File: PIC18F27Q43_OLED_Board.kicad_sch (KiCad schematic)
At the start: 29 parts, among them J1 Conn_PIC_ICSP_ICD, J2 OLED_Connector, J3 UART_Connector, SW1 SW_Push, SW2 SW_Push, SW3 SW_Push, SW4 SW_SPDT, SW5 SW_SPDT, SW6 SW_SPDT, SW7 SW_SPDT, U1 PIC18F27Q43-I/STX

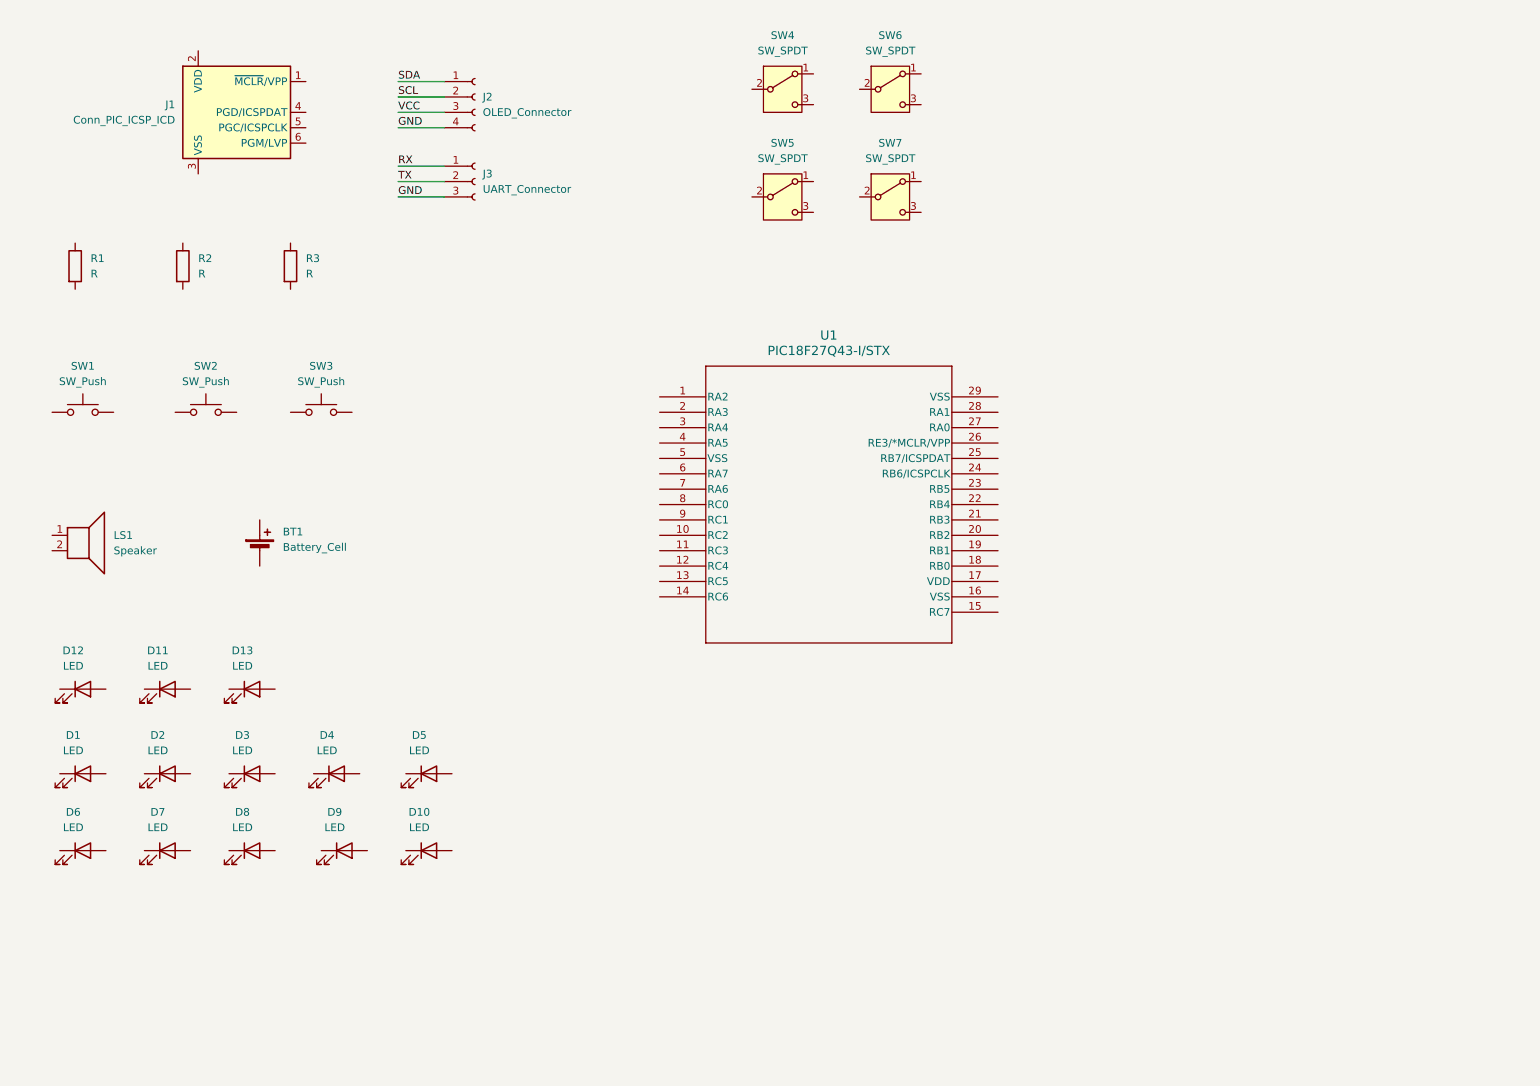
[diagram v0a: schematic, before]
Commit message: Finished SCHfor VEXT + VBAT
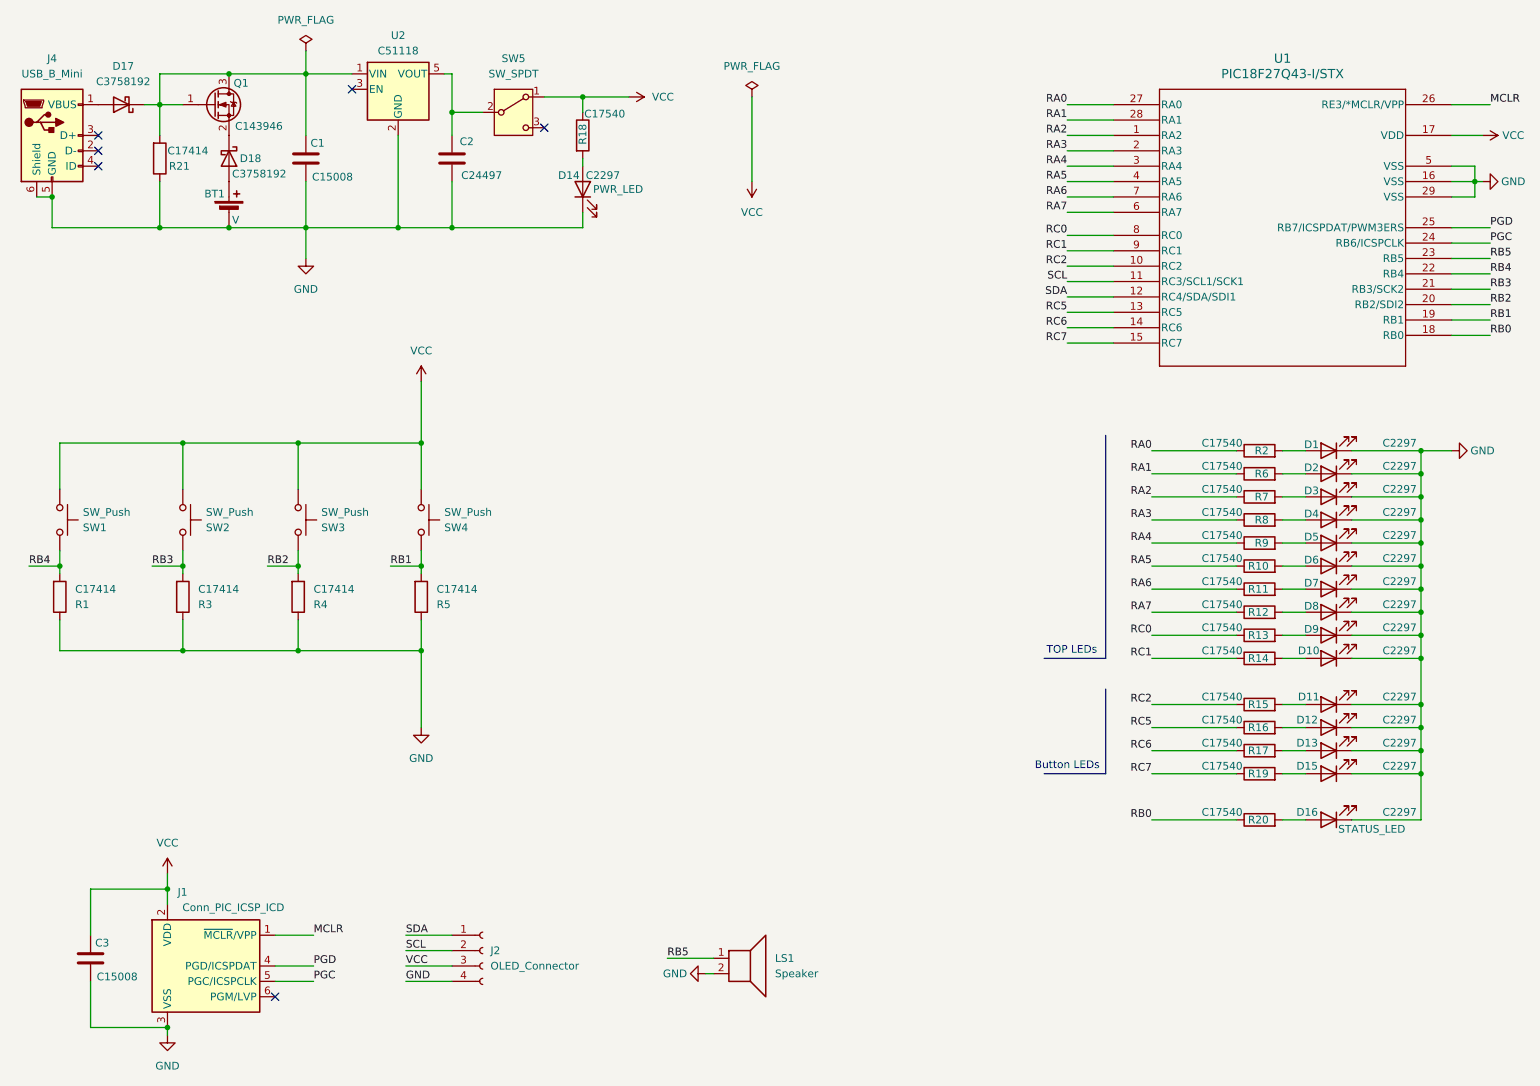
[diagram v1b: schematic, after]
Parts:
- removed J3: UART_Connector, symbol Connector:Conn_01x03_Socket
- removed SW5, SW6, SW7: SW_SPDT, symbol Switch:SW_SPDT
- added C1, C3: C15008, Capacitor_SMD:C_1206_3216Metric, symbol Device:C
- added C2: C24497, Capacitor_SMD:C_1206_3216Metric, symbol Device:C
- added D14, D15, D16: C2297, LED_0805_2012Metric, symbol Device:LED
- added D17, D18: C3758192, Diode_SMD:D_0603_1608Metric, symbol Device:D_Schottky
- added J4: USB_B_Mini, Connector_USB:USB_Mini-B_Tensility_54-00023_Vertical, symbol Connector:USB_B_Mini
- added Q1: C143946, Package_TO_SOT_SMD:SOT-23, symbol Transistor_FET:IRLML6244
- added R10, R11, R12, R13, R14, R15, R16, R17, R18, R19, R20, R6, R7, R8, R9: C17540, Resistor_SMD:R_0805_2012Metric, symbol Device:R
- added R21, R4, R5: C17414, Resistor_SMD:R_0805_2012Metric, symbol Device:R
- added SW4: SW_Push, Button_Switch_THT:SW_PUSH_6mm_H5mm, symbol Switch:SW_Push
- added U2: C51118, Package_TO_SOT_SMD:SOT-23-5, symbol Regulator_Linear:AP2112K-3.3
- BT1: value Battery_Cell -> V; footprint (none) -> Battery:BatteryHolder_ComfortableElectronic_CH273-2450_1x2450
- D1, D10, D11, D12, D13, D2, D3, D4, D5, D6, D7, D8, D9: value LED -> C2297; footprint (none) -> LED_0805_2012Metric
- J1: footprint (none) -> Connector_PinHeader_2.54mm:PinHeader_1x05_P2.54mm_Vertical
- J2: footprint (none) -> Connector_PinHeader_2.54mm:PinHeader_1x04_P2.54mm_Vertical
- LS1: footprint (none) -> Buzzer_Beeper:Buzzer_12x9.5RM7.6
- R1, R3: value R -> C17414; footprint (none) -> Resistor_SMD:R_0805_2012Metric
- R2: value R -> C17540; footprint (none) -> Resistor_SMD:R_0805_2012Metric
- SW1, SW2, SW3: footprint (none) -> Button_Switch_THT:SW_PUSH_6mm_H5mm
- SW5: renamed from SW4; footprint (none) -> Button_Switch_THT:SW_Slide_SPDT_Straight_CK_OS102011MS2Q
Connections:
- net GND: now also BT1.2 (-), D1.1 (K), D10.1 (K), D11.1 (K), D12.1 (K), D13.1 (K), D2.1 (K), D3.1 (K), D4.1 (K), D5.1 (K), D6.1 (K), D7.1 (K), D8.1 (K), D9.1 (K), J1.3 (VSS), LS1.2, R1.1, R3.1, U1.16 (VSS), U1.29 (VSS), U1.5 (VSS), C1.2, C2.2, C3.2, D14.1 (K), D15.1 (K), D16.1 (K), J4.5 (GND), J4.6 (Shield), R21.1, R4.1, R5.1, U2.2 (GND)
- net SCL: now also U1.11 (RC3/SCL1/SCK1)
- net SDA: now also U1.12 (RC4/SDA/SDI1)
- net VCC: now also J1.2 (VDD), SW1.2, SW2.2, SW3.2, SW5.1 (A), U1.17 (VDD), C3.1, R18.1, SW4.2
- net RB2: now reaches SW3.1
- net RB2: now also U1.20 (RB2/SDI2), R4.2
- net at D9.2 (A): now also R13.2
- net RB4: now reaches SW1.1
- net RB4: now also R1.2, U1.22 (RB4)
- net RA2: now reaches U1.1 (RA2)
- net RA2: now also R7.1
- net RC2: now reaches U1.10 (RC2)
- net RC2: now also R15.1
- net RC5: now reaches U1.13 (RC5)
- net RC5: now also R16.1
- net RC6: now reaches U1.14 (RC6)
- net RC6: now also R17.1
- net RC7: now reaches U1.15 (RC7)
- net RC7: now also R19.1
- net RB0: now reaches U1.18 (RB0)
- net RB0: now also R20.1
- net RB1: now reaches U1.19 (RB1)
- net RB1: now also R5.2, SW4.1
- net RA3: now reaches U1.2 (RA3)
- net RA3: now also R8.1
- net RB3: now reaches U1.21 (RB3/SCK2)
- net RB3: now also R3.2, SW2.1
- net RB5: now reaches U1.23 (RB5)
- net RB5: now also LS1.1
- net PGC: now reaches U1.24 (RB6/ICSPCLK)
- net PGC: now also J1.5 (PGC/ICSPCLK)
- net PGD: now reaches U1.25 (RB7/ICSPDAT/PWM3ERS)
- net PGD: now also J1.4 (PGD/ICSPDAT)
- net MCLR: now reaches U1.26 (RE3/*MCLR/VPP)
- net MCLR: now also J1.1 (~{MCLR}/VPP)
- net RA0: now reaches U1.27 (RA0)
- net RA0: now also R2.1
- net RA1: now reaches U1.28 (RA1)
- net RA1: now also R6.1
- net RA4: now reaches U1.3 (RA4)
- net RA4: now also R9.1
- net RA5: now reaches U1.4 (RA5)
- net RA5: now also R10.1
- net RA7: now reaches U1.6 (RA7)
- net RA7: now also R12.1
- net RA6: now reaches U1.7 (RA6)
- net RA6: now also R11.1
- net RC0: now reaches U1.8 (RC0)
- net RC0: now also R13.1
- net RC1: now reaches U1.9 (RC1)
- net RC1: now also R14.1
- net at D8.2 (A): now also R12.2
- net at D5.2 (A): now also R9.2
- net at D7.2 (A): now also R11.2
- net at D10.2 (A): now also R14.2
- net at D13.2 (A): now also R17.2
- net at BT1.1 (+): now also D18.2 (A)
- net at D2.2 (A): now also R6.2
- net at R2.2: now also D1.2 (A)
- net at D4.2 (A): now also R8.2
- net at D11.2 (A): now also R15.2
- net at D6.2 (A): now also R10.2
- net at D12.2 (A): now also R16.2
- net at D3.2 (A): now also R7.2
- net at SW5.2 (B): now also C2.1, U2.5 (VOUT)
- new net: D15.2 (A), R19.2
- new net: D16.2 (A), R20.2
- new net: D14.2 (A), R18.2
- new net: D18.1 (K), Q1.2 (S)
- new net: C1.1, D17.1 (K), Q1.1 (G), Q1.3 (D), R21.2, U2.1 (VIN)
- new net: D17.2 (A), J4.1 (VBUS)
- no-connect marks 0 -> 6
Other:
- note added: "Button LEDs"
- note added: "TOP LEDs"
- moved on the sheet: BT1, D1, J1, J2, LS1, R1, R2, SW1, SW2, SW3, SW5, U1

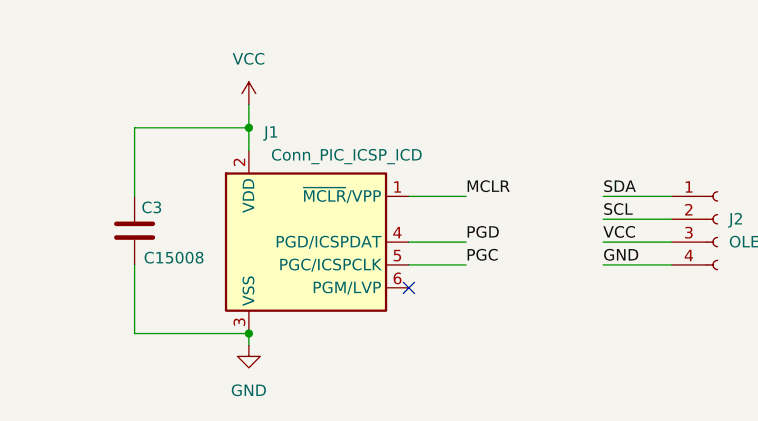
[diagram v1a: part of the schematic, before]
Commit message: Refine Silkscreen
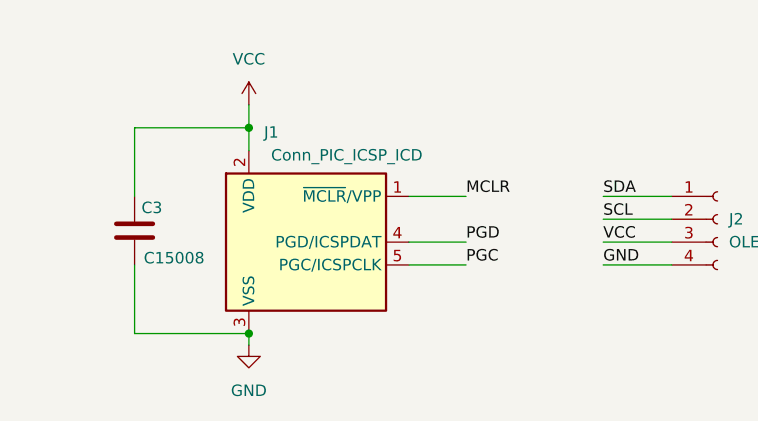
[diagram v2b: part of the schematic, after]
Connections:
- no-connect marks 6 -> 5
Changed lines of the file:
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@@
 	)
 	(no_connect
-		(at 62.23 179.07)
-	)
-	(no_connect
 		(at 74.93 29.21)
 	)
@@
 		(pin "5"
 		)
-		(pin "6"
-		)
 		(pin "4"

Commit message: Ready for PCBA
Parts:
- U1: value PIC18F27Q43-I/STX -> C638193
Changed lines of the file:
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@@
 		(dnp no)
 		(property "Reference" "U1"
-			(at 228.6 24.13 0)
+			(at 247.65 22.098 0)
 			(effects
 				(font
@@
 			)
 		)
-		(property "Value" "PIC18F27Q43-I/STX"
-			(at 228.6 26.67 0)
+		(property "Value" "C638193"
+			(at 244.094 24.892 0)
 			(effects
 				(font
@@
 		)
 		(property "Datasheet" "PIC18F27Q43-I/STX"
-			(at 200.66 36.83 0)
+			(at 239.014 27.178 0)
 			(effects
 				(font
@@
 					(italic yes)
 				)
-				(hide yes)
 			)
 		)
-		(property "Description" ""
+		(property "Description" "PIC18F27Q43-I/STX"
 			(at 200.66 34.29 0)
 			(effects

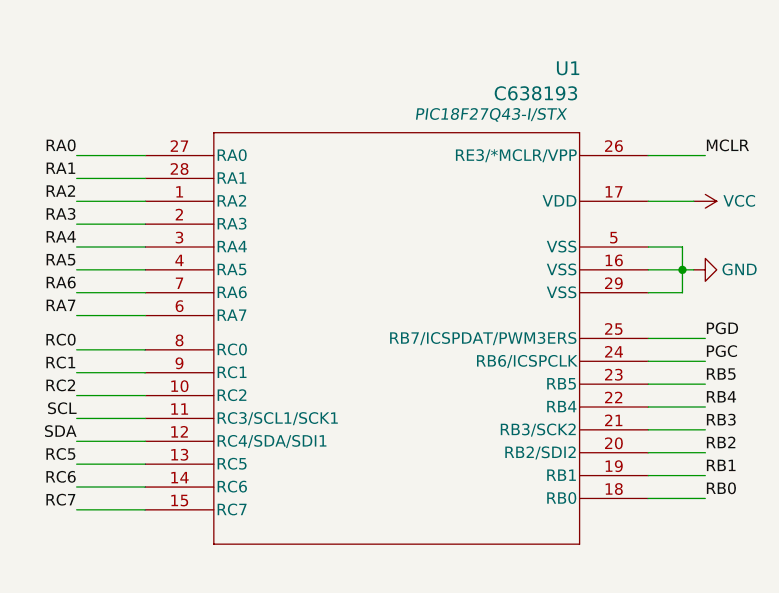
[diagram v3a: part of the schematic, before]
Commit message: move from Q43 -> Q84 due to chip shortage
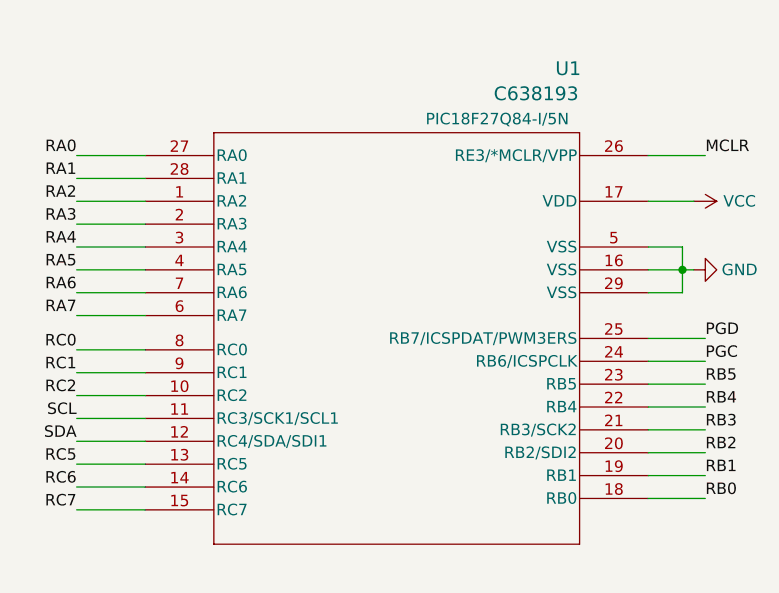
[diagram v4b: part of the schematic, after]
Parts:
- U1: footprint VQFN28_STX_MCH -> VQFN28_5N_MCH; symbol PIC18F27Q43-I-STX:PIC18F27Q43-I_STX -> 2025-03-28_09-28-23:PIC18F27Q84-I_5N
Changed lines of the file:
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@@
 	)
 	(symbol
-		(lib_id "PIC18F27Q43-I-STX:PIC18F27Q43-I_STX")
+		(lib_id "2025-03-28_09-28-23:PIC18F27Q84-I_5N")
 		(at 200.66 34.29 0)
 		(unit 1)
@@
 			)
 		)
-		(property "Footprint" "VQFN28_STX_MCH"
+		(property "Footprint" "VQFN28_5N_MCH"
 			(at 200.66 36.83 0)
 			(effects
@@
 			)
 		)
-		(property "Datasheet" "PIC18F27Q43-I/STX"
-			(at 239.014 27.178 0)
+		(property "Datasheet" "PIC18F27Q84-I/5N"
+			(at 239.522 77.216 0)
 			(effects
 				(font
@@
 					(italic yes)
 				)
+				(hide yes)
 			)
 		)
-		(property "Description" "PIC18F27Q43-I/STX"
-			(at 200.66 34.29 0)
+		(property "Description" "PIC18F27Q84-I/5N"
+			(at 239.776 27.686 0)
 			(effects
 				(font
 					(size 1.27 1.27)
 				)
-				(hide yes)
 			)
 		)

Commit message: update symbol
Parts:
- J1, J2, LS1: now left out of the parts list
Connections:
- no-connect marks 5 -> 6
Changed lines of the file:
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@@
 	)
 	(no_connect
+		(at 62.23 179.07)
+	)
+	(no_connect
 		(at 106.68 35.56)
 	)
@@
 		(unit 1)
 		(exclude_from_sim yes)
-		(in_bom yes)
+		(in_bom no)
 		(on_board yes)
 		(dnp no)
@@
 		(unit 1)
 		(exclude_from_sim yes)
-		(in_bom yes)
+		(in_bom no)
 		(on_board yes)
 		(dnp no)
@@
 		(unit 1)
 		(exclude_from_sim yes)
-		(in_bom yes)
+		(in_bom no)
 		(on_board yes)
 		(dnp no)
@@
 		(pin "1"
 		)
+		(pin "6"
+		)
 		(instances
